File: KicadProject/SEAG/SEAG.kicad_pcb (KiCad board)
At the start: 2 copper layers, 99.6 x 99.1 mm, 37 parts, among them J2 Conn_01x06_Pin, U1 STM32F722RCTx, U3 SGTL5000XNAA3

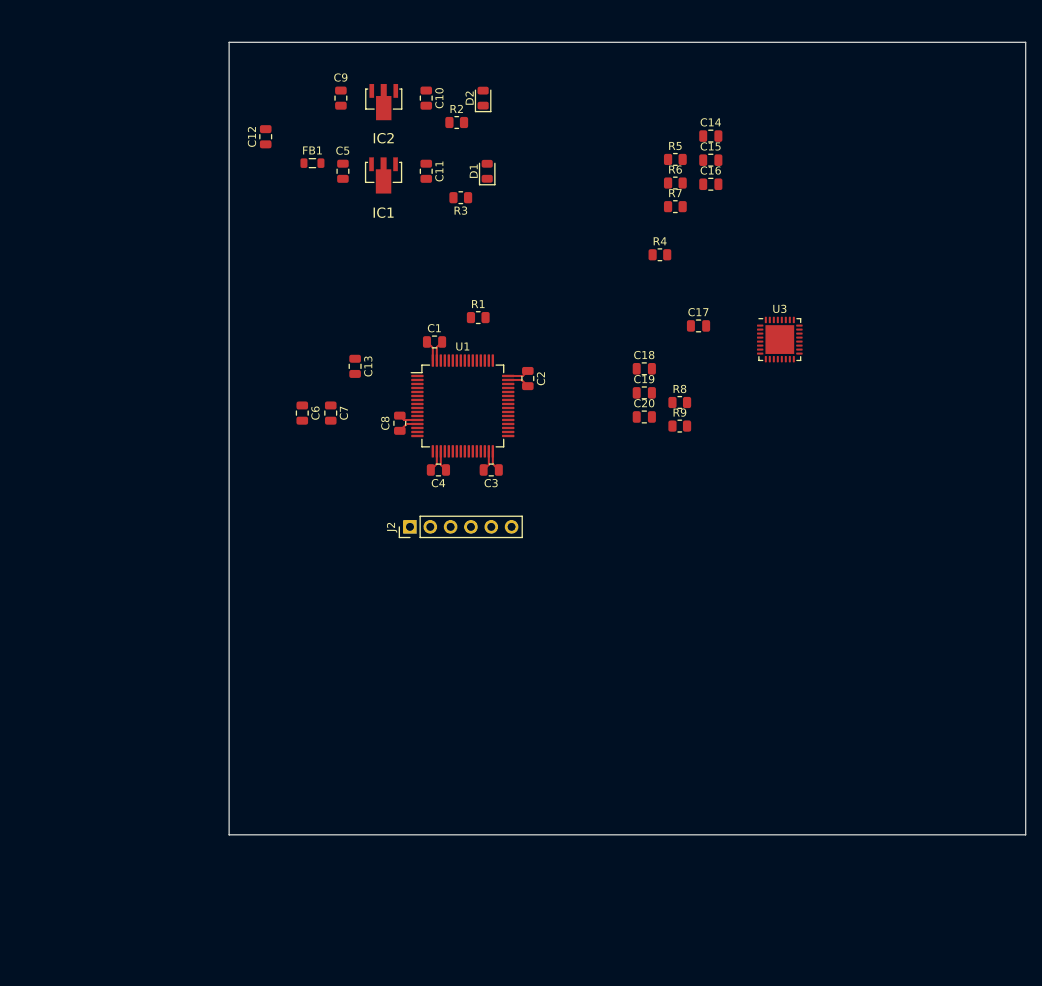
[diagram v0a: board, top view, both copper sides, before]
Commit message: Added ESD protection, extra filtering with ferrite bead
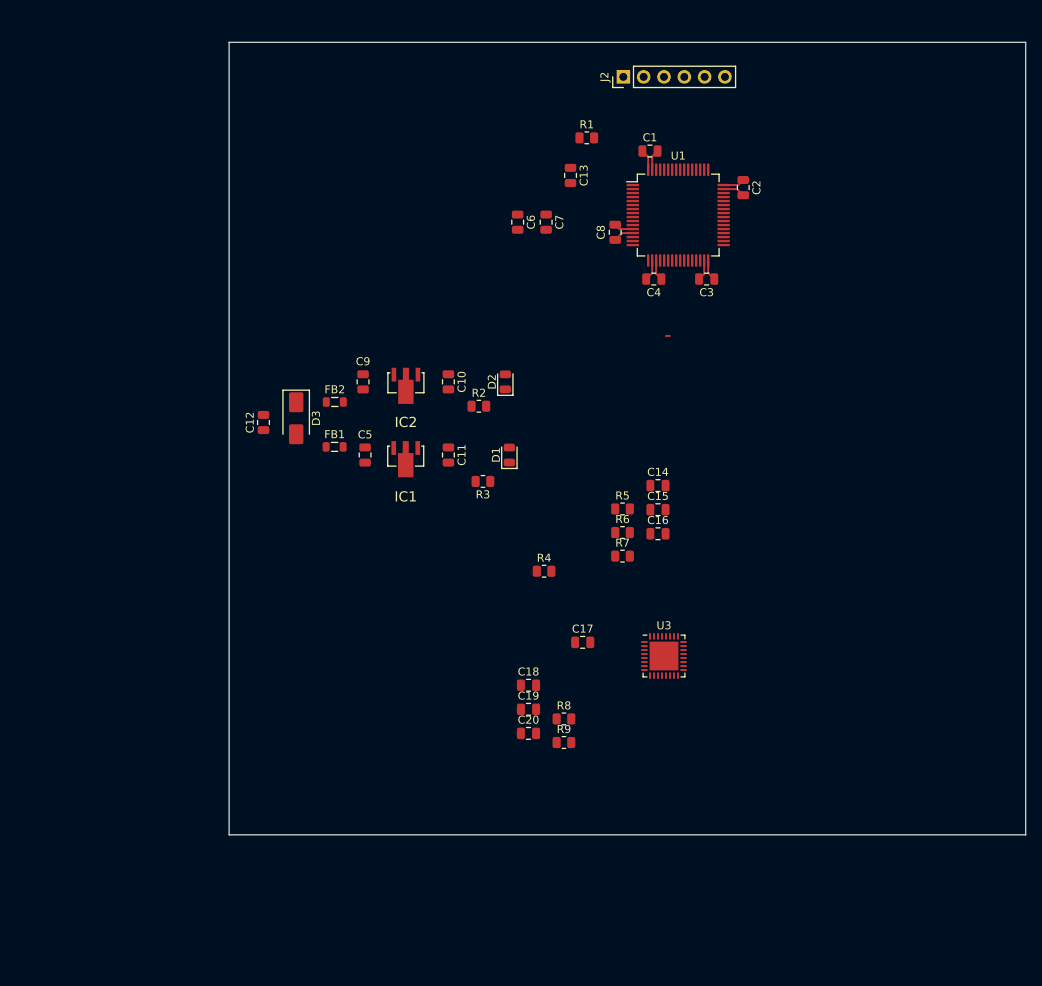
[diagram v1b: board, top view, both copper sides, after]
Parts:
- added D3: SMAJ6.5A, Diode_SMD:D_SMA, F.Cu at (85.3, 83.6)
- added FB2: 600R, Inductor_SMD:L_0805_2012Metric, F.Cu at (90.2, 81.5)
- R4: value 10K -> 9K
- moved J2 62.3 mm to (126.2, 40.9)
- moved R5 44.2 mm to (126.1, 94.9)
- moved C14 44.2 mm to (130.6, 92.0)
- moved C16 44.2 mm to (130.6, 98.0)
- moved R6 44.2 mm to (126.1, 97.9)
- moved R7 44.2 mm to (126.1, 100.8)
- moved C15 44.2 mm to (130.6, 95.0)
- moved R4 42.1 mm to (116.3, 102.7)
- moved C19 42.1 mm to (114.4, 119.9)
- moved C20 42.1 mm to (114.4, 123.0)
- moved R8 42.1 mm to (118.8, 121.1)
- moved R9 42.1 mm to (118.8, 124.1)
- moved U3 42.1 mm to (131.3, 113.3)
- moved C17 42.1 mm to (121.2, 111.6)
- moved C18 42.1 mm to (114.4, 116.9)
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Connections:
- net Net-(U1-BOOT0) renamed /MCU/BOOT0
- C12 pad 1: Net-(IC2-IN) -> Net-(D3-A1)
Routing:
- net /MCU/SWCLK: track 0.00 -> 0.63 mm
- added copper zone on In1.Cu, net GND
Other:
- copper layers 2 -> 4

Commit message: Finished PCB, stil uncertain about couple things
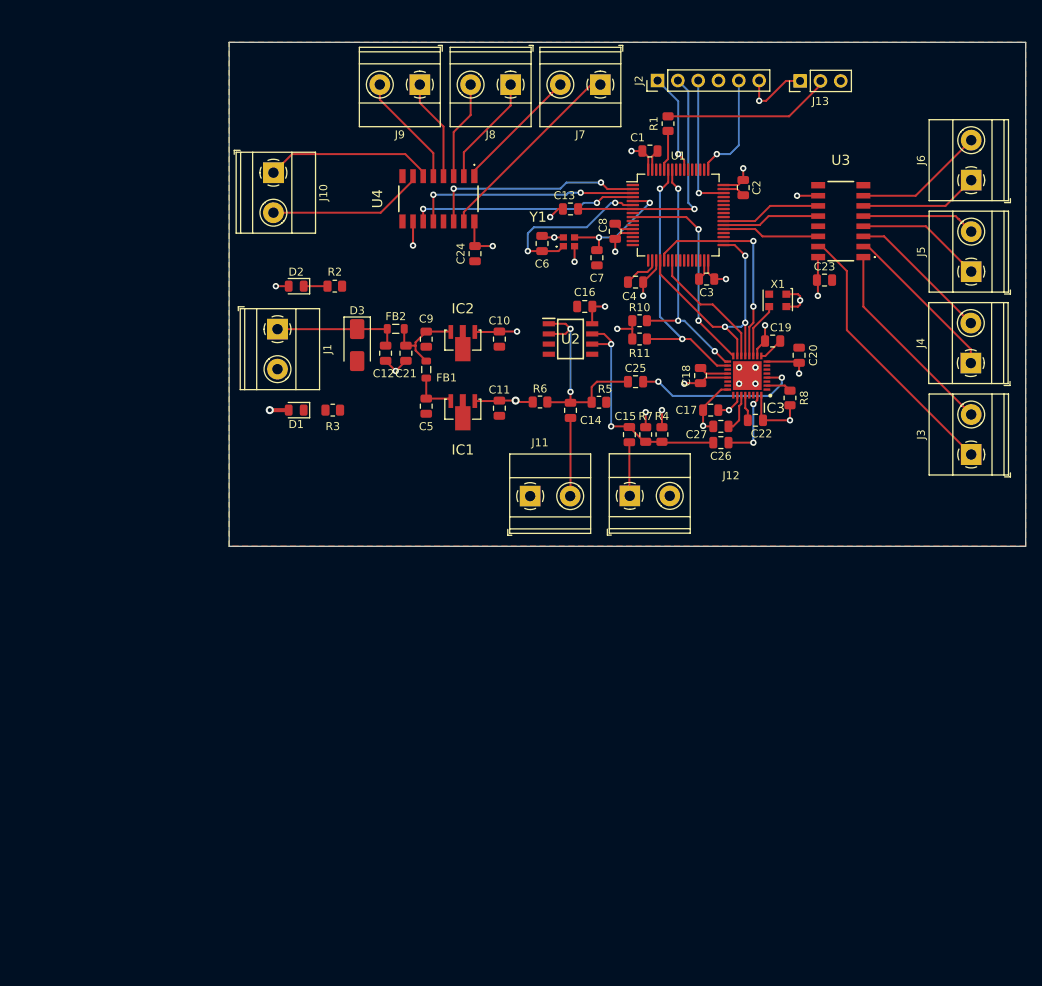
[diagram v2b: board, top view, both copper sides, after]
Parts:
- removed R9: 10K, Resistor_SMD:R_0805_2012Metric
- added C21: 2u2, Capacitor_SMD:C_0805_2012Metric, F.Cu at (99.1, 75.4)
- added C22: 100n, Capacitor_SMD:C_0805_2012Metric, F.Cu at (142.7, 83.8)
- added C23: 100n, Capacitor_SMD:C_0805_2012Metric, F.Cu at (151.4, 66.3)
- added C24: 100n, Capacitor_SMD:C_0805_2012Metric, F.Cu at (107.7, 63.0)
- added C25: 1u, Capacitor_SMD:C_0805_2012Metric, F.Cu at (127.8, 79.0)
- added C26: 100u, Capacitor_SMD:C_0805_2012Metric, F.Cu at (138.4, 86.6)
- added C27: 4.7u, Capacitor_SMD:C_0805_2012Metric, F.Cu at (138.4, 84.6)
- added IC3: ~, SamacSys_Parts:QFN50P500X500X100-33N, F.Cu at (141.7, 78.2)
- added J1: Screw_Terminal_01x02, TerminalBlock_Phoenix:TerminalBlock_Phoenix_MKDS-1,5-2_1x02_P5.00mm_Horizontal, F.Cu at (83.0, 72.4)
- added J10: Screw_Terminal_01x02, TerminalBlock_Phoenix:TerminalBlock_Phoenix_MKDS-1,5-2_1x02_P5.00mm_Horizontal, F.Cu at (82.5, 52.9)
- added J11: Screw_Terminal_01x02, TerminalBlock_Phoenix:TerminalBlock_Phoenix_MKDS-1,5-2_1x02_P5.00mm_Horizontal, F.Cu at (114.6, 93.3)
- added J12: Screw_Terminal_01x02, TerminalBlock_Phoenix:TerminalBlock_Phoenix_MKDS-1,5-2_1x02_P5.00mm_Horizontal, F.Cu at (127.0, 93.3)
- added J13: Conn_01x03_Pin, Connector_PinHeader_2.54mm:PinHeader_1x03_P2.54mm_Vertical, F.Cu at (148.3, 41.4)
- added J3: Screw_Terminal_01x02, TerminalBlock_Phoenix:TerminalBlock_Phoenix_MKDS-1,5-2_1x02_P5.00mm_Horizontal, F.Cu at (169.7, 88.1)
- added J4: Screw_Terminal_01x02, TerminalBlock_Phoenix:TerminalBlock_Phoenix_MKDS-1,5-2_1x02_P5.00mm_Horizontal, F.Cu at (169.7, 76.7)
- added J5: Screw_Terminal_01x02, TerminalBlock_Phoenix:TerminalBlock_Phoenix_MKDS-1,5-2_1x02_P5.00mm_Horizontal, F.Cu at (169.7, 65.2)
- added J6: Screw_Terminal_01x02, TerminalBlock_Phoenix:TerminalBlock_Phoenix_MKDS-1,5-2_1x02_P5.00mm_Horizontal, F.Cu at (169.7, 53.8)
- added J7: Screw_Terminal_01x02, TerminalBlock_Phoenix:TerminalBlock_Phoenix_MKDS-1,5-2_1x02_P5.00mm_Horizontal, F.Cu at (123.4, 41.9)
- added J8: Screw_Terminal_01x02, TerminalBlock_Phoenix:TerminalBlock_Phoenix_MKDS-1,5-2_1x02_P5.00mm_Horizontal, F.Cu at (112.1, 41.9)
- added J9: Screw_Terminal_01x02, TerminalBlock_Phoenix:TerminalBlock_Phoenix_MKDS-1,5-2_1x02_P5.00mm_Horizontal, F.Cu at (100.8, 41.9)
- added R10: 10K, Resistor_SMD:R_0805_2012Metric, F.Cu at (128.3, 71.4)
- added R11: 10K, Resistor_SMD:R_0805_2012Metric, F.Cu at (128.3, 73.7)
- added U2: ~, SamacSys_Parts:SOIC127P600X175-8N, F.Cu at (119.6, 73.7)
- added U4: ~, SamacSys_Parts:74HC595DQ100118, F.Cu at (103.1, 56.1)
- added X1: XO32, Oscillator:Oscillator_SMD_EuroQuartz_XO32-4Pin_3.2x2.5mm, F.Cu at (145.5, 68.8)
- added Y1: Crystal_GND24, SamacSys_Parts:FW2500025Z, F.Cu at (119.4, 61.5)
- C15: value 100µ -> 100n
- C17: value 10n -> 4u7
- C18: value 10u -> 4u7
- R4: value 9K -> 100K
- R7: value 1K -> 100K
- R8: value 10K -> 33k
- U3: value SGTL5000XNAA3 -> ~; footprint Package_DFN_QFN:QFN-32-1EP_5x5mm_P0.5mm_EP3.6x3.6mm -> SamacSys_Parts:74HC595DQ100118
- moved U3 58.7 mm to (153.4, 58.9), turned to 180 degrees
- moved C20 58.1 mm to (148.2, 75.7), turned to 90 degrees
- moved C19 55.2 mm to (144.9, 73.9)
- moved R8 49.1 mm to (147.1, 81.0), turned to 90 degrees
- moved C18 44.3 mm to (135.9, 78.2), turned to 90 degrees
- moved C17 33.1 mm to (137.2, 82.5), turned to 180 degrees
- moved C16 29.8 mm to (121.4, 69.6), turned to 180 degrees
- moved D2 28.7 mm to (85.3, 67.1), turned to 180 degrees
- moved D1 27.2 mm to (85.3, 82.5), turned to 180 degrees
- moved R2 23.4 mm to (90.2, 67.1), turned to 180 degrees
- moved R4 22.6 mm to (131.1, 85.6), turned to 90 degrees
- moved R3 20.8 mm to (89.9, 82.5)
- moved R6 19.3 mm to (115.8, 81.5)
- moved C12 17.5 mm to (96.5, 75.4), turned to -90 degrees
- moved R7 15.5 mm to (129.0, 85.6), turned to 90 degrees
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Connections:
- C14 pad 1: AudioIn -> /AudioFiltering/AudioIn
- C14 pad 2: Net-(U2-+) -> AudioInFilt
- C15 pad 1: Net-(C15-Pad1) -> AudioOut
- C15 pad 2: GND -> Net-(J12-Pin_1)
- R4 pad 1: Net-(U2--) -> AudioOut
- R4 pad 2: AudioInFilt -> +3.3VA
- R5 pad 1: Net-(U2-+) -> AudioInFilt
- R6 pad 2: Net-(U2-+) -> AudioInFilt
- R7 pad 1: Net-(U2--) -> AudioOut
- R7 pad 2: Net-(C15-Pad1) -> GND
- R8 pad 1: GND -> +3.3VA
- R8 pad 2: Net-(U3-LINEIN_L) -> Net-(IC3-LINPUT3/JD2)
- U1 pad 2: unconnected-(U1-PC13-Pad2) -> ShiftRegFDat
- U1 pad 20: unconnected-(U1-PA4-Pad20) -> I2S.WS
- U1 pad 21: unconnected-(U1-PA5-Pad21) -> I2S.CLK
- U1 pad 23: unconnected-(U1-PA7-Pad23) -> I2S.DSD
- U1 pad 3: unconnected-(U1-PC14-Pad3) -> ShiftRegFClk
- U1 pad 33: unconnected-(U1-PB12-Pad33) -> I2S.WS
- U1 pad 34: unconnected-(U1-PB13-Pad34) -> I2S.CLK
- U1 pad 37: unconnected-(U1-PC6-Pad37) -> ShiftRegBarDat
- U1 pad 38: unconnected-(U1-PC7-Pad38) -> ShiftRegBarClk
- U1 pad 39: unconnected-(U1-PC8-Pad39) -> ShiftRegBarStoClk
- U1 pad 4: unconnected-(U1-PC15-Pad4) -> ShiftRegFStoClk
- U1 pad 58: unconnected-(U1-PB6-Pad58) -> I2C.SCL
- U1 pad 59: unconnected-(U1-PB7-Pad59) -> I2C.SDA
- U1 pad 9: unconnected-(U1-PC1-Pad9) -> I2S.ASD
- U3 pad 1: GND -> /IO/Q1b
- U3 pad 10: unconnected-(U3-VAG-Pad10) -> +3V3
- U3 pad 11: AudioOut -> ShiftRegBarStoClk
- U3 pad 12: Net-(U3-LINEOUT_L) -> ShiftRegBarClk
- U3 pad 13: AudioFiltIn -> GND
- U3 pad 14: Net-(U3-LINEIN_L) -> ShiftRegBarDat
- U3 pad 15: unconnected-(U3-MIC-Pad15) -> /IO/Q0b
- U3 pad 16: unconnected-(U3-MIC_BIAS-Pad16) -> +3V3
- U3 pad 2: unconnected-(U3-HP_R-Pad2) -> /IO/Q2b
- U3 pad 3: GND -> /IO/Q3b
- U3 pad 4: unconnected-(U3-HP_VGND-Pad4) -> /IO/Q4b
- U3 pad 5: +3.3VA -> /IO/Q5b
- U3 pad 6: unconnected-(U3-HP_L-Pad6) -> /IO/Q6b
- U3 pad 7: GND -> /IO/Q7b
- U3 pad 8: unconnected-(U3-NC-Pad8) -> GND
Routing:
- net +3.3VA: track 2.55 -> 127.6 mm, vias 0 -> 8
- net +3V3: track 10.6 -> 69.5 mm, vias 0 -> 16
- net I2S.WS: track 0.00 -> 35.4 mm, vias 0 -> 3
- net I2C.SDA: track 0.00 -> 34.4 mm, vias 0 -> 2
- net /IO/Q0b: track 0.00 -> 34.2 mm
- net /MCU/NRST: track 0.00 -> 31.5 mm, vias 0 -> 1
- net I2C.SCL: track 0.00 -> 31.4 mm, vias 0 -> 3
- net GND: track 13.0 -> 43.4 mm, vias 0 -> 9
- net AudioOut: track 0.00 -> 29.6 mm, vias 0 -> 2
- net ShiftRegFClk: track 0.00 -> 28.4 mm, vias 0 -> 2
- net ShiftRegFStoClk: track 0.00 -> 28.4 mm, vias 0 -> 2
- net AudioInFilt: track 0.00 -> 28.0 mm, vias 0 -> 2
- net I2S.CLK: track 0.00 -> 27.2 mm, vias 0 -> 2
- net ShiftRegFDat: track 0.00 -> 27.1 mm, vias 0 -> 2
- net I2S.ASD: track 0.00 -> 26.5 mm, vias 0 -> 2
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- added copper zone on In2.Cu, net +3V3
- added copper zone on F.Cu, net GND
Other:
- board size 99.6 x 99.1 mm -> 99.6 x 63 mm

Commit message: PCB rev 2
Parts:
- removed J10, J8, J9: Screw_Terminal_01x02, TerminalBlock_Phoenix:TerminalBlock_Phoenix_MKDS-1,5-2_1x02_P5.00mm_Horizontal
- removed J13: Conn_01x03_Pin, Connector_PinHeader_2.54mm:PinHeader_1x03_P2.54mm_Vertical
- removed R8: 33k, Resistor_SMD:R_0805_2012Metric
- removed X1: XO32, Oscillator:Oscillator_SMD_EuroQuartz_XO32-4Pin_3.2x2.5mm
- added C305: 100n, Capacitor_SMD:C_0805_2012Metric, F.Cu at (123.1, 119.6)
- added C309: 4.7u, Capacitor_SMD:C_0805_2012Metric, F.Cu at (105.8, 116.7)
- added C603: 100n, Capacitor_SMD:C_0805_2012Metric, F.Cu at (127.0, 97.5)
- added C604: 100n, Capacitor_SMD:C_0805_2012Metric, F.Cu at (134.6, 97.5)
- added C605: 100n, Capacitor_SMD:C_0805_2012Metric, F.Cu at (109.2, 97.5)
- added C606: 100n, Capacitor_SMD:C_0805_2012Metric, F.Cu at (116.8, 97.5)
- added C607: 100n, Capacitor_SMD:C_0805_2012Metric, F.Cu at (134.6, 140.7)
- added C608: 100n, Capacitor_SMD:C_0805_2012Metric, F.Cu at (127.0, 140.7)
- added C609: 100n, Capacitor_SMD:C_0805_2012Metric, F.Cu at (116.8, 140.7)
- added C610: 100n, Capacitor_SMD:C_0805_2012Metric, F.Cu at (109.2, 140.7)
- added H1: MountingHole, MountingHole:MountingHole_3mm, F.Cu at (55.9, 91.4)
- added H2: MountingHole, MountingHole:MountingHole_3mm, F.Cu at (55.9, 147.3)
- added H3: MountingHole, MountingHole:MountingHole_3mm, F.Cu at (144.8, 91.4)
- added H4: MountingHole, MountingHole:MountingHole_3mm, F.Cu at (144.8, 147.3)
- added J14: Screw_Terminal_01x08, SamacSys_Parts:1725711, F.Cu at (144.8, 116.8)
- added R501: 33k, Resistor_SMD:R_0805_2012Metric, F.Cu at (85.6, 118.4)
- added R601: 10K, Resistor_SMD:R_0805_2012Metric, F.Cu at (124.5, 97.5)
- added R602: 10K, Resistor_SMD:R_0805_2012Metric, F.Cu at (132.1, 97.5)
- added R603: 10K, Resistor_SMD:R_0805_2012Metric, F.Cu at (106.7, 97.5)
- added R604: 10K, Resistor_SMD:R_0805_2012Metric, F.Cu at (114.3, 97.5)
- added R605: 10K, Resistor_SMD:R_0805_2012Metric, F.Cu at (137.2, 140.7)
- added R606: 10K, Resistor_SMD:R_0805_2012Metric, F.Cu at (129.5, 140.7)
- added R607: 10K, Resistor_SMD:R_0805_2012Metric, F.Cu at (119.4, 140.7)
- added R608: 10K, Resistor_SMD:R_0805_2012Metric, F.Cu at (111.8, 140.7)
- J3: value Screw_Terminal_01x02 -> Screw_Terminal_01x08; footprint TerminalBlock_Phoenix:TerminalBlock_Phoenix_MKDS-1,5-2_1x02_P5.00mm_Horizontal -> SamacSys_Parts:1725711
- J4, J5, J6, J7: value Screw_Terminal_01x02 -> Screw_Terminal_01x06; footprint TerminalBlock_Phoenix:TerminalBlock_Phoenix_MKDS-1,5-2_1x02_P5.00mm_Horizontal -> SamacSys_Parts:1725698
- moved J2 114.0 mm to (88.4, 147.3)
- moved J7 105.5 mm to (119.4, 147.3)
- moved J6 99.0 mm to (137.2, 147.3), turned to 180 degrees
- moved U4 82.6 mm to (135.4, 132.1), turned to 180 degrees
- moved R301 81.5 mm to (124.5, 127.9), turned to -135 degrees
- moved C303 80.3 mm to (112.8, 129.8), turned to -135 degrees
- moved C602 75.7 mm to (129.0, 135.6), turned to 90 degrees
- moved C304 73.9 mm to (122.1, 123.7), turned to -135 degrees
- moved C502 71.1 mm to (89.4, 115.8), turned to 0 degrees
- moved J12 68.9 mm to (58.4, 99.1), turned to -90 degrees
- moved J5 68.3 mm to (106.7, 91.4), turned to 0 degrees
- moved C505 66.9 mm to (81.3, 110.3), turned to 90 degrees
- moved C401 66.4 mm to (66.5, 106.9), turned to -90 degrees
- moved C501 65.9 mm to (91.4, 112.5), turned to -90 degrees
- moved C506 65.5 mm to (76.2, 119.4)
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- renumbered C12 to C201, C21 to C202, C9 to C203, C10 to C204, C5 to C205, C11 to C206, C4 to C301, C3 to C302, C2 to C303, C1 to C304, C8 to C306, C6 to C307, C7 to C308, C16 to C401, C14 to C402, C15 to C403, C19 to C501, C20 to C502, C18 to C503, C17 to C504, C22 to C505, C25 to C506, C27 to C507, C26 to C508, C23 to C601, C24 to C602, R2 to R201, R3 to R202, R1 to R301, R10 to R302, R11 to R303, R6 to R401, R5 to R402, R4 to R403, R7 to R404
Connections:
- IC3 pad 11: /Codec/OscOut -> MCLK
- J3 pad 1: /IO/Q0b -> /IO/Q0l
- J3 pad 2: /IO/Q1b -> /IO/Q1l
- J4 pad 1: /IO/Q2b -> Net-(J4-Pin_1)
- J4 pad 2: /IO/Q3b -> ToggleInput1
- J5 pad 1: /IO/Q4b -> Net-(J5-Pin_1)
- J5 pad 2: /IO/Q5b -> ToggleInput3
- J6 pad 1: /IO/Q6b -> Net-(J6-Pin_1)
- J6 pad 2: /IO/Q7b -> ToggleInput5
- J7 pad 1: /IO/Q0l -> Net-(J7-Pin_1)
- J7 pad 2: /IO/Q1l -> ToggleInput7
- R202 pad 1: GND -> Net-(D1-K)
- R202 pad 2: Net-(D1-K) -> GND
- R301 pad 1: Net-(J13-Pin_2) -> GND
- U1 pad 10: unconnected-(U1-PC2-Pad10) -> ShiftRegBarClk
- U1 pad 11: unconnected-(U1-PC3-Pad11) -> ShiftRegBarStoClk
- U1 pad 24: unconnected-(U1-PC4-Pad24) -> MCLK
- U1 pad 30: unconnected-(U1-VCAP_1-Pad30) -> Net-(U1-VCAP_1)
- U1 pad 37: ShiftRegBarDat -> unconnected-(U1-PC6-Pad37)
- U1 pad 38: ShiftRegBarClk -> unconnected-(U1-PC7-Pad38)
- U1 pad 39: ShiftRegBarStoClk -> unconnected-(U1-PC8-Pad39)
- U1 pad 42: unconnected-(U1-PA9-Pad42) -> ToggleInput2
- U1 pad 43: unconnected-(U1-PA10-Pad43) -> ToggleInput1
- U1 pad 44: unconnected-(U1-PA11-Pad44) -> ToggleInput4
- U1 pad 45: unconnected-(U1-PA12-Pad45) -> ToggleInput3
- U1 pad 50: unconnected-(U1-PA15-Pad50) -> ToggleInput8
- U1 pad 51: unconnected-(U1-PC10-Pad51) -> ToggleInput7
- U1 pad 52: unconnected-(U1-PC11-Pad52) -> ToggleInput6
- U1 pad 53: unconnected-(U1-PC12-Pad53) -> ToggleInput5
- U1 pad 8: unconnected-(U1-PC0-Pad8) -> ShiftRegBarDat
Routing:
- net ToggleInput2: track 0.00 -> 63.0 mm
- net ToggleInput1: track 0.00 -> 57.6 mm
- net ToggleInput3: track 0.00 -> 53.8 mm
- net ToggleInput4: track 0.00 -> 53.6 mm
- net +3.3VA: track 127.6 -> 175.4 mm, vias 8 -> 10
- net ToggleInput5: track 0.00 -> 31.9 mm
- net /MCU/SWO: track 12.5 -> 42.1 mm
- net ToggleInput8: track 0.00 -> 26.5 mm
- net ToggleInput6: track 0.00 -> 26.3 mm
- net ToggleInput7: track 0.00 -> 23.5 mm
- net MCLK: track 0.00 -> 23.4 mm, vias 0 -> 2
- net Net-(J13-Pin_2): track 21.2 -> 0.00 mm
- net I2C.SCL: track 31.4 -> 52.1 mm, vias 3 -> 2
- net /MCU/NRST: track 31.5 -> 51.7 mm
- net /IO/Q0b: track 34.2 -> 15.1 mm
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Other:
- board size 99.6 x 63 mm -> 99.1 x 66.1 mm
- board text added: "+"
- board text added: "-"
- board text added: "3V3"
- board text added: "5V"
- board text added: "Audio In"
- board text added: "Audio Out"
- board text added: "GND"
- board text added: "RST"
- board text added: "SEAG"
- board text added: "SWC"
- board text added: "SWD"
- board text added: "SWO"
